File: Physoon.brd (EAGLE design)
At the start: 100 x 80 mm, 37 parts, among them IC2 74AHC1G125DBV, IC3 74AHC1G125DBV, M1 HX1, X1 BU-SMA-V

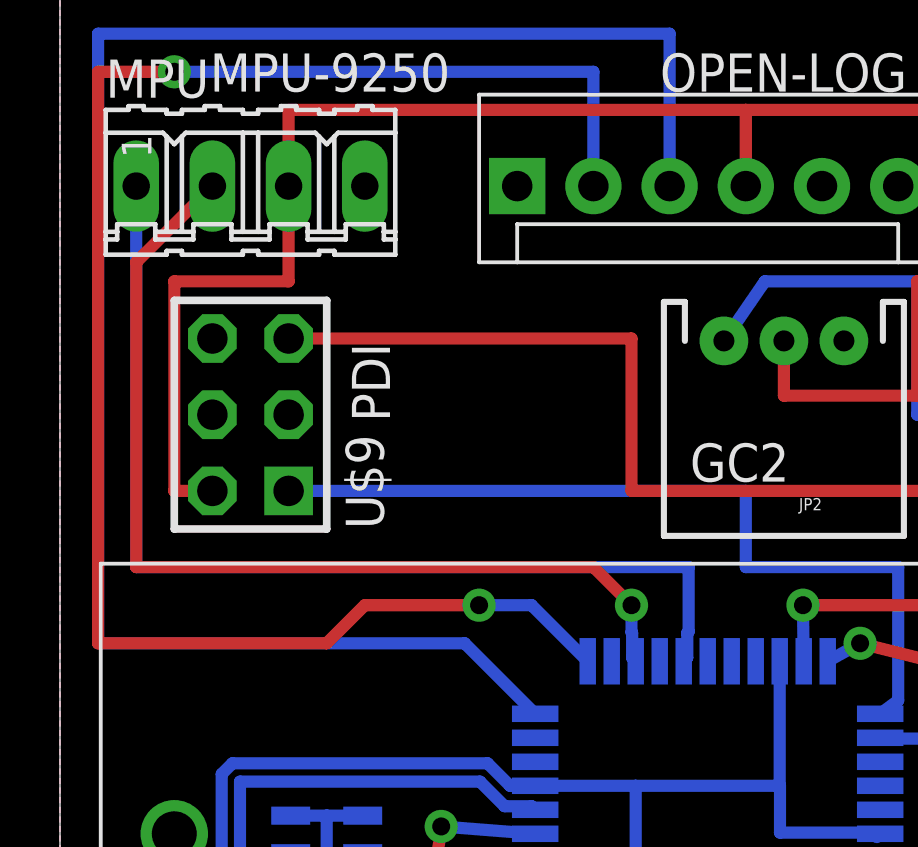
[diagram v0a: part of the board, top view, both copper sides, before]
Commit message: fix interface for IMU
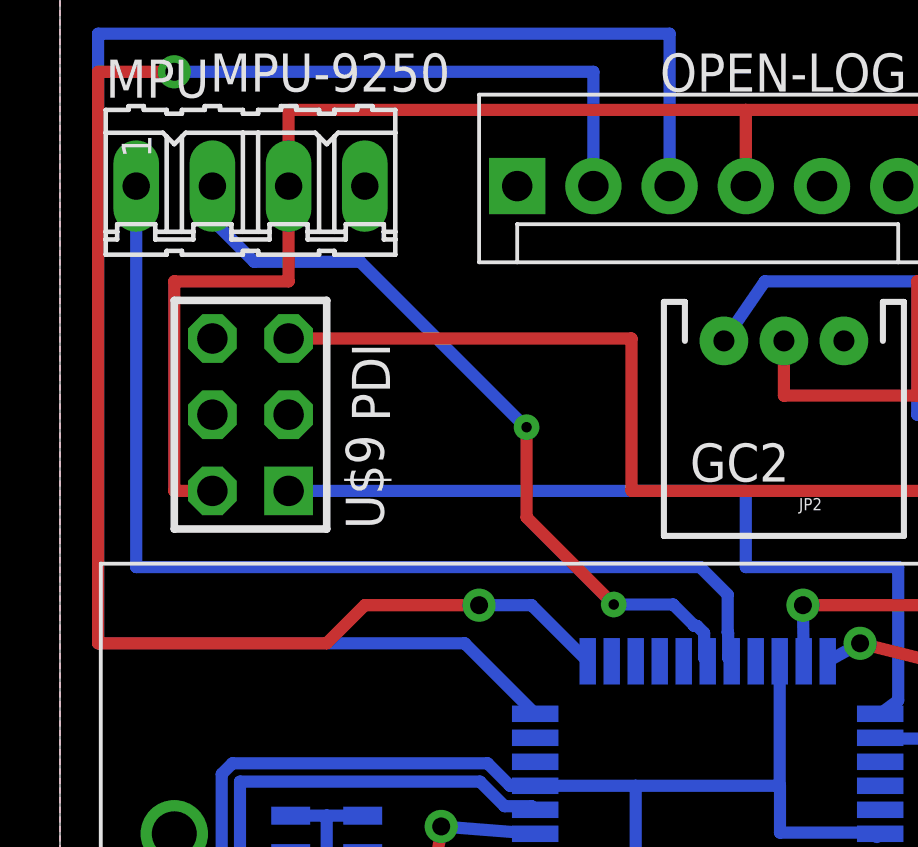
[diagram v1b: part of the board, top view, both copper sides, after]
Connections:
- removed net SCLKD: IC1.27, MPU.1
- removed net SDID: IC1.25, MPU.2
- new net SCLE: IC1.29, MPU.1
- new net SDAD: IC1.28, MPU.2
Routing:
- net SCLE: track 0.00 -> 35.1 mm
- net SCLKD: track 34.3 -> 0.00 mm
- net SDID: track 32.7 -> 0.00 mm, vias 1 -> 0
- net SDAD: track 0.00 -> 26.2 mm, vias 0 -> 2
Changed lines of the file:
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@@
 <?xml version="1.0" encoding="utf-8"?>
 <!DOCTYPE eagle SYSTEM "eagle.dtd">
-<eagle version="8.1.1">
+<eagle version="8.2.0">
 <drawing>
 <settings>
@@
 <via x="18" y="45" extent="1-16" drill="0.6"/>
 <contactref element="LED1" pad="C"/>
+<wire x1="27.34" y1="49.06" x2="23.19" y2="54.01" width="0" layer="19" extent="16-16"/>
 </signal>
 <signal name="PDI-DATA">
@@
 <wire x1="57.15" y1="53.34" x2="63.5" y2="59.69" width="0.4064" layer="16"/>
 </signal>
-<signal name="SDID">
-<contactref element="IC1" pad="25"/>
-<contactref element="MPU" pad="2"/>
-<wire x1="5.08" y1="69.85" x2="2.54" y2="67.31" width="0.4064" layer="1"/>
-<wire x1="2.54" y1="67.31" x2="2.54" y2="57.15" width="0.4064" layer="1"/>
-<wire x1="2.54" y1="57.15" x2="17.78" y2="57.15" width="0.4064" layer="1"/>
-<wire x1="17.78" y1="57.15" x2="19.05" y2="55.88" width="0.4064" layer="1"/>
-<via x="19.05" y="55.88" extent="1-16" drill="0.6"/>
-<wire x1="19.05" y1="55.88" x2="19.05" y2="54.9747375" width="0.4064" layer="16"/>
-<wire x1="19.05" y1="54.9747375" x2="19.0714" y2="54.9533375" width="0.4064" layer="16"/>
-<wire x1="19.0714" y1="54.9533375" x2="19.0714" y2="54.1286" width="0.4064" layer="16"/>
-<wire x1="19.0714" y1="54.1286" x2="19.19" y2="54.01" width="0.4064" layer="16"/>
-</signal>
-<signal name="SCLKD">
-<contactref element="IC1" pad="27"/>
+<signal name="SCLE">
 <contactref element="MPU" pad="1"/>
 <wire x1="2.54" y1="69.85" x2="2.54" y2="57.15" width="0.4064" layer="16"/>
-<wire x1="20.955" y1="57.15" x2="20.955" y2="54.9997375" width="0.4064" layer="16"/>
-<wire x1="20.955" y1="54.9997375" x2="20.9086" y2="54.9533375" width="0.4064" layer="16"/>
-<wire x1="20.9086" y1="54.9533375" x2="20.9086" y2="54.1286" width="0.4064" layer="16"/>
-<wire x1="20.9086" y1="54.1286" x2="20.79" y2="54.01" width="0.4064" layer="16"/>
-<wire x1="2.54" y1="57.15" x2="20.955" y2="57.15" width="0.4064" layer="16"/>
+<contactref element="IC1" pad="29"/>
+<wire x1="21.338540625" y1="57.15" x2="22.25548125" y2="56.233059375" width="0.4064" layer="16"/>
+<wire x1="22.25548125" y1="56.233059375" x2="22.25548125" y2="54.96925625" width="0.4064" layer="16"/>
+<wire x1="22.25548125" y1="54.96925625" x2="22.2714" y2="54.9533375" width="0.4064" layer="16"/>
+<wire x1="22.2714" y1="54.9533375" x2="22.2714" y2="54.1286" width="0.4064" layer="16"/>
+<wire x1="22.2714" y1="54.1286" x2="22.39" y2="54.01" width="0.4064" layer="16"/>
+<wire x1="2.54" y1="57.15" x2="21.338540625" y2="57.15" width="0.4064" layer="16"/>
 </signal>
 <signal name="THERM">
@@
 <wire x1="44.375" y1="75.005" x2="43.18" y2="76.2" width="0.4064" layer="16"/>
 </signal>
+<signal name="SDAD">
+<contactref element="MPU" pad="2"/>
+<contactref element="IC1" pad="28"/>
+<wire x1="5.08" y1="69.85" x2="5.08" y2="68.7197" width="0.4064" layer="16"/>
+<wire x1="5.08" y1="68.7197" x2="6.47191875" y2="67.32778125" width="0.4064" layer="16"/>
+<wire x1="6.47191875" y1="67.32778125" x2="10.00505625" y2="67.32778125" width="0.4064" layer="16"/>
+<wire x1="10.00505625" y1="67.32778125" x2="15.55241875" y2="61.78041875" width="0.4064" layer="16"/>
+<wire x1="15.55241875" y1="61.78041875" x2="15.55241875" y2="61.813440625" width="0.4064" layer="16"/>
+<via x="15.55241875" y="61.813440625" extent="1-16" drill="0.35"/>
+<wire x1="15.55241875" y1="61.813440625" x2="15.55241875" y2="58.80861875" width="0.4064" layer="1"/>
+<wire x1="15.55241875" y1="58.80861875" x2="18.52421875" y2="55.83681875" width="0.4064" layer="1"/>
+<wire x1="18.52421875" y1="55.83681875" x2="18.52421875" y2="55.836821875" width="0.4064" layer="1"/>
+<wire x1="18.52421875" y1="55.836821875" x2="18.45818125" y2="55.902859375" width="0.4064" layer="1"/>
+<via x="18.45818125" y="55.902859375" extent="1-16" drill="0.35"/>
+<wire x1="18.45818125" y1="55.902859375" x2="20.43938125" y2="55.902859375" width="0.4064" layer="16"/>
+<wire x1="20.43938125" y1="55.902859375" x2="21.1328" y2="55.209440625" width="0.4064" layer="16"/>
+<wire x1="21.1328" y1="55.209440625" x2="21.1328" y2="55.1914" width="0.4064" layer="16"/>
+<wire x1="21.2333375" y1="55.1914" x2="21.4714" y2="54.9533375" width="0.4064" layer="16"/>
+<wire x1="21.4714" y1="54.9533375" x2="21.4714" y2="54.1286" width="0.4064" layer="16"/>
+<wire x1="21.4714" y1="54.1286" x2="21.59" y2="54.01" width="0.4064" layer="16"/>
+<wire x1="21.1328" y1="55.209440625" x2="21.150840625" y2="55.1914" width="0.4064" layer="16"/>
+<wire x1="21.150840625" y1="55.1914" x2="21.2333375" y2="55.1914" width="0.4064" layer="16"/>
+</signal>
 </signals>
